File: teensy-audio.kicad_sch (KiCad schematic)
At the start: 44 parts, among them J1 AudioJack2, J2 AudioJack2, J3 Barrel_Jack, J4 Conn_02x08_Odd_Even, J5 Conn_02x08_Odd_Even, J6 Conn_02x05_Odd_Even, J7 Conn_01x04, SW1 RotaryEncoder_Switch, SW2 SW_Push, SW3 SW_Push, SW4 SW_Push, SW5 SW_Push, U1 LM358, U2 LM7805_TO220, U3 Teensy4.0, U4 Teensy4.0_AudioShield_REVD

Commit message: added power connectors
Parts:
- added J10: Conn_01x05, Connector_PinHeader_2.54mm:PinHeader_1x05_P2.54mm_Vertical, symbol Connector_Generic:Conn_01x05
- added J8: Conn_01x04, Connector_PinHeader_2.54mm:PinHeader_1x04_P2.54mm_Vertical, symbol Connector_Generic:Conn_01x04
- added J9: Conn_02x05_Odd_Even, Connector_PinHeader_2.54mm:PinHeader_2x05_P2.54mm_Vertical, symbol Connector_Generic:Conn_02x05_Odd_Even
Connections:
- net +3.3V: now also J9.1 (Pin_1), J9.3 (Pin_3), J9.5 (Pin_5), J9.7 (Pin_7), J9.9 (Pin_9)
- net +5V: now also J9.10 (Pin_10), J9.2 (Pin_2), J9.4 (Pin_4), J9.6 (Pin_6), J9.8 (Pin_8)
- net GND: now also J10.1 (Pin_1), J10.2 (Pin_2), J10.3 (Pin_3), J10.4 (Pin_4), J10.5 (Pin_5)
- net MISO: now also J8.3 (Pin_3)
- net MOSI: now also J8.2 (Pin_2)
- net SCK: now also J8.4 (Pin_4)
- net SDCS: now also J8.1 (Pin_1)

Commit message: finished pcb
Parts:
- J1, J2: footprint Connector_Audio:Jack_6.35mm_Neutrik_NMJ4HFD2_Horizontal -> Connector_Audio:Jack_6.35mm_Neutrik_NMJ6HFD2-AU_Horizontal
- J3: footprint Connector_BarrelJack:BarrelJack_CUI_PJ-063AH_Horizontal -> Connector_BarrelJack:BarrelJack_GCT_DCJ200-10-A_Horizontal
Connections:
- net GND: now also J3.1; no longer J3.2
- net VCC: now also J3.2; no longer J3.1
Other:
- moved on the sheet: J3
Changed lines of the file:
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@@
     (stroke (width 0) (type default))
   )
-  (wire (pts (xy 154.94 34.29) (xy 158.75 34.29))
-    (stroke (width 0) (type default))
-  )
   (wire (pts (xy 133.35 151.13) (xy 139.7 151.13))
     (stroke (width 0) (type default))
@@
     (stroke (width 0) (type default))
   )
-  (wire (pts (xy 261.62 31.75) (xy 261.62 34.29))
+  (wire (pts (xy 261.62 33.02) (xy 261.62 34.29))
     (stroke (width 0) (type default))
   )
@@
     (stroke (width 0) (type default))
   )
+  (wire (pts (xy 261.62 24.13) (xy 261.62 27.94))
+    (stroke (width 0) (type default))
+  )
   (wire (pts (xy 123.19 87.63) (xy 123.19 96.52))
     (stroke (width 0) (type default))
@@
     (stroke (width 0) (type default))
   )
-  (wire (pts (xy 261.62 26.67) (xy 261.62 24.13))
-    (stroke (width 0) (type default))
-  )
   (wire (pts (xy 274.32 77.47) (xy 278.13 77.47))
     (stroke (width 0) (type default))
@@
     (stroke (width 0) (type default))
   )
+  (wire (pts (xy 261.62 27.94) (xy 267.97 27.94))
+    (stroke (width 0) (type default))
+  )
   (wire (pts (xy 92.71 91.44) (xy 92.71 93.98))
     (stroke (width 0) (type default))
@@
     (stroke (width 0) (type default))
   )
-  (wire (pts (xy 179.07 99.06) (xy 182.88 99.06))
+  (wire (pts (xy 154.94 34.29) (xy 158.75 34.29))
     (stroke (width 0) (type default))
   )
-  (wire (pts (xy 259.08 26.67) (xy 261.62 26.67))
+  (wire (pts (xy 179.07 99.06) (xy 182.88 99.06))
     (stroke (width 0) (type default))
   )
@@
     (stroke (width 0) (type default))
   )
+  (wire (pts (xy 267.97 33.02) (xy 261.62 33.02))
+    (stroke (width 0) (type default))
+  )
   (wire (pts (xy 130.81 83.82) (xy 130.81 81.28))
     (stroke (width 0) (type default))
@@
     (stroke (width 0) (type default))
   )
-  (wire (pts (xy 259.08 31.75) (xy 261.62 31.75))
-    (stroke (width 0) (type default))
-  )
   (wire (pts (xy 182.88 73.66) (xy 168.91 73.66))
     (stroke (width 0) (type default))
@@
     )
   )
-  (symbol (lib_id "Connector:Barrel_Jack") (at 251.46 29.21 0) (unit 1)
+  (symbol (lib_id "Connector:Barrel_Jack") (at 275.59 30.48 180) (unit 1)
     (in_bom yes) (on_board yes) (dnp no) (fields_autoplaced)
-    (property "Reference" "J3" (at 251.46 20.32 0)
-      (effects (font (size 1.27 1.27)))
+    (property "Reference" "J3" (at 281.94 29.21 0)
+      (effects (font (size 1.27 1.27)) (justify right))
     )
-    (property "Value" "Barrel_Jack" (at 251.46 22.86 0)
-      (effects (font (size 1.27 1.27)))
+    (property "Value" "Barrel_Jack" (at 281.94 31.75 0)
+      (effects (font (size 1.27 1.27)) (justify right))
     )
-    (property "Footprint" "Connector_BarrelJack:BarrelJack_CUI_PJ-063AH_Horizontal" (at 252.73 30.226 0)
+    (property "Footprint" "Connector_BarrelJack:BarrelJack_GCT_DCJ200-10-A_Horizontal" (at 274.32 29.464 0)
       (effects (font (size 1.27 1.27)) hide)
     )
-    (property "Datasheet" "~" (at 252.73 30.226 0)
+    (property "Datasheet" "~" (at 274.32 29.464 0)
       (effects (font (size 1.27 1.27)) hide)
     )
@@
       (effects (font (size 1.27 1.27)))
     )
-    (property "Footprint" "Connector_Audio:Jack_6.35mm_Neutrik_NMJ4HFD2_Horizontal" (at 24.13 24.13 0)
+    (property "Footprint" "Connector_Audio:Jack_6.35mm_Neutrik_NMJ6HFD2-AU_Horizontal" (at 24.13 24.13 0)
       (effects (font (size 1.27 1.27)) hide)
     )
@@
       (effects (font (size 1.27 1.27)))
     )
-    (property "Footprint" "Connector_Audio:Jack_6.35mm_Neutrik_NMJ4HFD2_Horizontal" (at 166.37 34.29 0)
+    (property "Footprint" "Connector_Audio:Jack_6.35mm_Neutrik_NMJ6HFD2-AU_Horizontal" (at 166.37 34.29 0)
       (effects (font (size 1.27 1.27)) hide)
     )

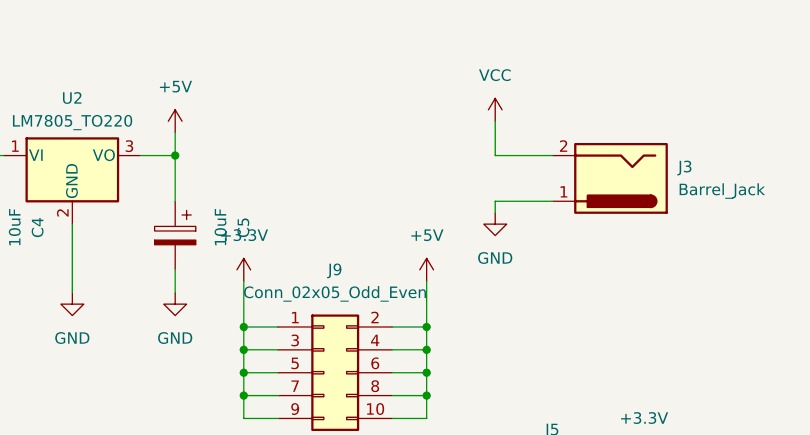
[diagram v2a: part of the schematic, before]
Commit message: added input power pins
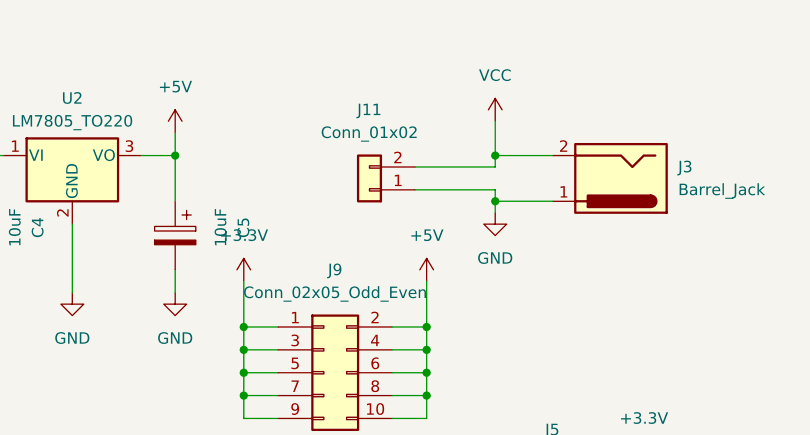
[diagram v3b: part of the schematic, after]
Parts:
- added J11: Conn_01x02, Connector_PinHeader_2.54mm:PinHeader_1x02_P2.54mm_Vertical, symbol Connector_Generic:Conn_01x02
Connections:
- net GND: now also J11.1 (Pin_1)
- net VCC: now also J11.2 (Pin_2)
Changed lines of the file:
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@@
   (junction (at 31.75 66.04) (diameter 0) (color 0 0 0 0)
   )
+  (junction (at 261.62 33.02) (diameter 0) (color 0 0 0 0)
+  )
   (junction (at 27.94 161.29) (diameter 0) (color 0 0 0 0)
   )
@@
   (junction (at 72.39 36.83) (diameter 0) (color 0 0 0 0)
   )
+  (junction (at 261.62 27.94) (diameter 0) (color 0 0 0 0)
+  )
   (junction (at 237.49 64.77) (diameter 0) (color 0 0 0 0)
   )
@@
     (stroke (width 0) (type default))
   )
+  (wire (pts (xy 252.73 31.75) (xy 261.62 31.75))
+    (stroke (width 0) (type default))
+  )
   (wire (pts (xy 22.86 182.88) (xy 26.67 182.88))
     (stroke (width 0) (type default))
@@
     (stroke (width 0) (type default))
   )
+  (wire (pts (xy 252.73 29.21) (xy 261.62 29.21))
+    (stroke (width 0) (type default))
+  )
   (wire (pts (xy 238.76 149.86) (xy 254 149.86))
     (stroke (width 0) (type default))
@@
     (stroke (width 0) (type default))
   )
+  (wire (pts (xy 261.62 29.21) (xy 261.62 27.94))
+    (stroke (width 0) (type default))
+  )
   (wire (pts (xy 38.1 161.29) (xy 33.02 161.29))
     (stroke (width 0) (type default))
@@
     (stroke (width 0) (type default))
   )
+  (wire (pts (xy 261.62 31.75) (xy 261.62 33.02))
+    (stroke (width 0) (type default))
+  )
   (wire (pts (xy 134.62 87.63) (xy 135.89 87.63))
     (stroke (width 0) (type default))
@@
   )
   (symbol (lib_id "teensy4.0_audioshield_revd:Teensy4.0_AudioShield_REVD") (at 105.41 154.94 0) (unit 1)
-    (in_bom yes) (on_board yes) (dnp no) (fields_autoplaced)
+    (in_bom yes) (on_board no) (dnp no) (fields_autoplaced)
     (property "Reference" "U4" (at 105.41 113.03 0)
       (effects (font (size 1.27 1.27)))
@@
         )
       )
+    )
+  )
+  (symbol (lib_id "Connector_Generic:Conn_01x02") (at 247.65 31.75 180) (unit 1)
+    (in_bom yes) (on_board yes) (dnp no) (fields_autoplaced)
+    (property "Reference" "J11" (at 247.65 22.86 0)
+      (effects (font (size 1.27 1.27)))
+    )
+    (property "Value" "Conn_01x02" (at 247.65 25.4 0)
+      (effects (font (size 1.27 1.27)))
+    )
+    (property "Footprint" "Connector_PinHeader_2.54mm:PinHeader_1x02_P2.54mm_Vertical" (at 247.65 31.75 0)
+      (effects (font (size 1.27 1.27)) hide)
+    )
+    (property "Datasheet" "~" (at 247.65 31.75 0)
+      (effects (font (size 1.27 1.27)) hide)
+    )
+    (pin "1")
+    (pin "2")
+    (instances
+      (project "teensy-audio"
+        (path "/6ae84b48-cfd0-4085-8818-9f5b4e5692b2"
+          (reference "J11") (unit 1)
+        )
+      )

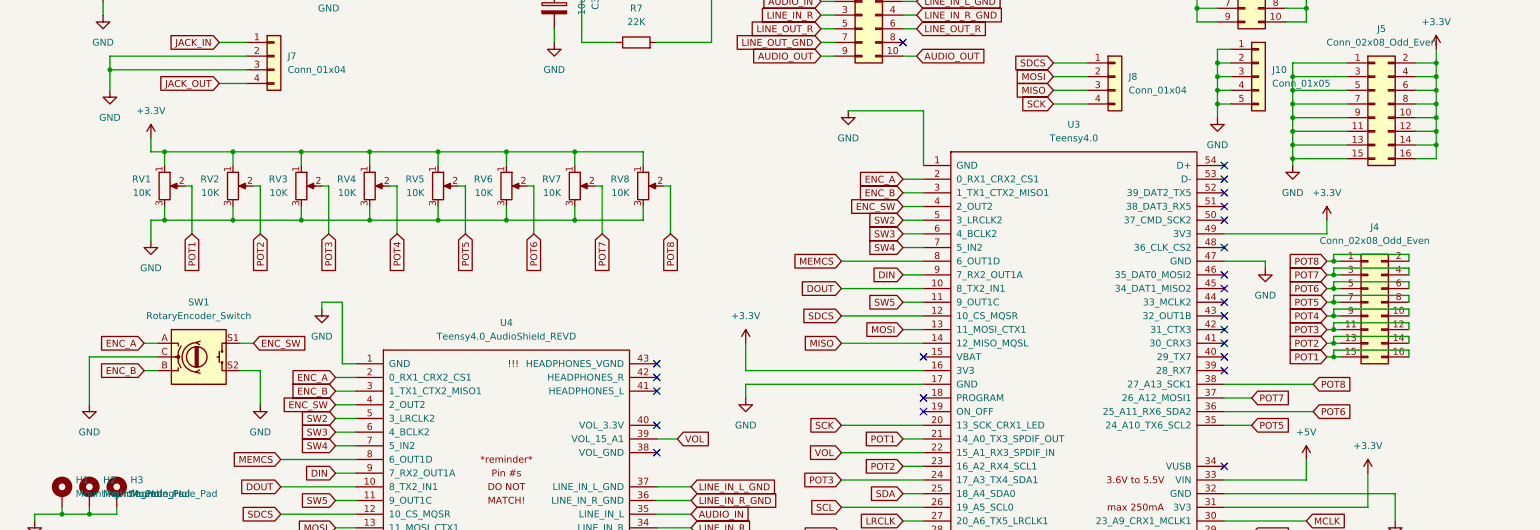
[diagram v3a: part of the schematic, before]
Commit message: added oled screen
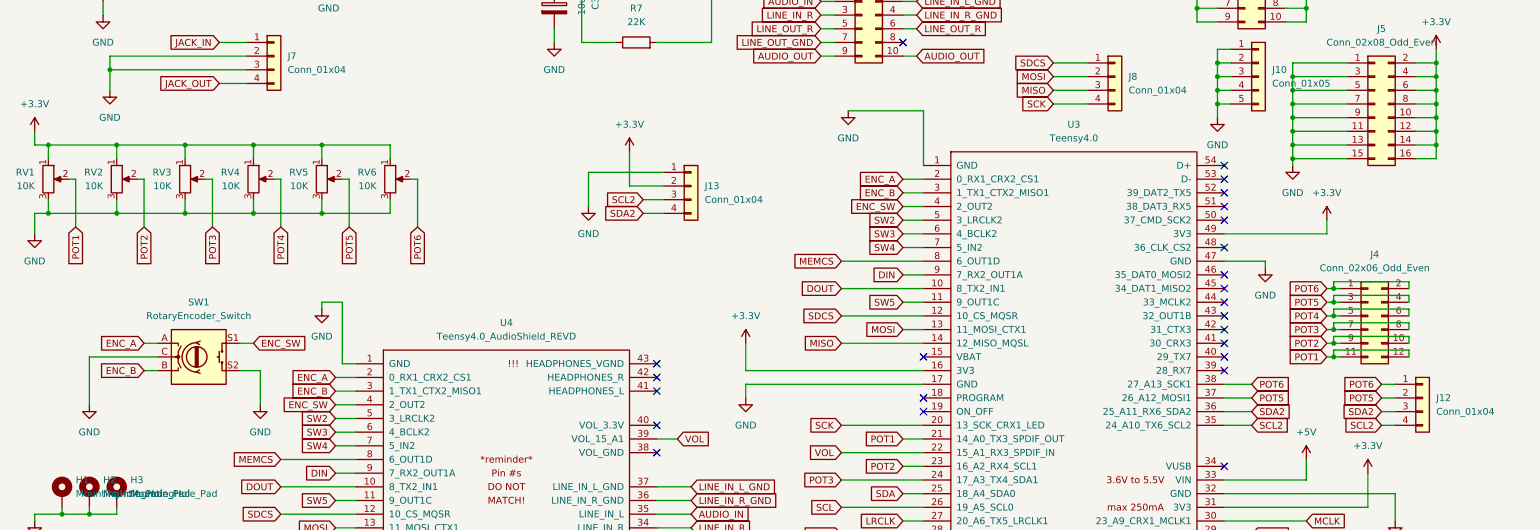
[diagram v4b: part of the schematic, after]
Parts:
- removed J4: Conn_02x08_Odd_Even, Connector_PinHeader_2.54mm:PinHeader_2x08_P2.54mm_Vertical, symbol Connector_Generic:Conn_02x08_Odd_Even
- removed RV7, RV8: 10K, Potentiometer_THT:Potentiometer_Bourns_PTV09A-1_Single_Vertical, symbol Device:R_Potentiometer
- added J12, J13: Conn_01x04, Connector_PinHeader_2.54mm:PinHeader_1x04_P2.54mm_Vertical, symbol Connector_Generic:Conn_01x04
- added J4: Conn_02x06_Odd_Even, Connector_PinHeader_2.54mm:PinHeader_2x06_P2.54mm_Vertical, symbol Connector_Generic:Conn_02x06_Odd_Even
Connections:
- net POT7 is gone; now on net POT5: U3.37 (26_A12_MOSI1)
- net POT8 is gone; now on net POT6: U3.38 (27_A13_SCK1)
- net +3.3V: now also J13.2 (Pin_2)
- net GND: now also J13.1 (Pin_1)
- net POT1: now also J4.11 (Pin_11), J4.12 (Pin_12)
- net POT2: now also J4.10 (Pin_10), J4.9 (Pin_9)
- net POT3: now also J4.7 (Pin_7), J4.8 (Pin_8)
- net POT4: now also J4.5 (Pin_5), J4.6 (Pin_6)
- net POT5: now also J12.2 (Pin_2), J4.3 (Pin_3), J4.4 (Pin_4); no longer U3.35 (24_A10_TX6_SCL2)
- net POT6: now also J12.1 (Pin_1), J4.1 (Pin_1), J4.2 (Pin_2); no longer U3.36 (25_A11_RX6_SDA2)
- new net SCL2: J12.4 (Pin_4), J13.3 (Pin_3), U3.35 (24_A10_TX6_SCL2)
- new net SDA2: J12.3 (Pin_3), J13.4 (Pin_4), U3.36 (25_A11_RX6_SDA2)
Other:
- moved on the sheet: RV1, RV2, RV3, RV4, RV5, RV6

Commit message: split audio and digital grounds
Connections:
- net LINE_IN_R_GND is gone; now on net GNDA: J6.4 (Pin_4), U4.36 (LINE_IN_R_GND)
- net LINE_OUT_GND is gone; now on net GNDA: J6.7 (Pin_7), U4.32 (LINE_OUT_GND)
- net GND: no longer C3.2, J1.S, J2.S, J7.2 (Pin_2), J7.3 (Pin_3), R2.2, R4.2, R5.2, U1.4 (V-)
- net LINE_IN_L_GND renamed GNDA
- net GNDA: now also C3.2, J1.S, J2.S, J7.2 (Pin_2), J7.3 (Pin_3), R2.2, R4.2, R5.2, U1.4 (V-)

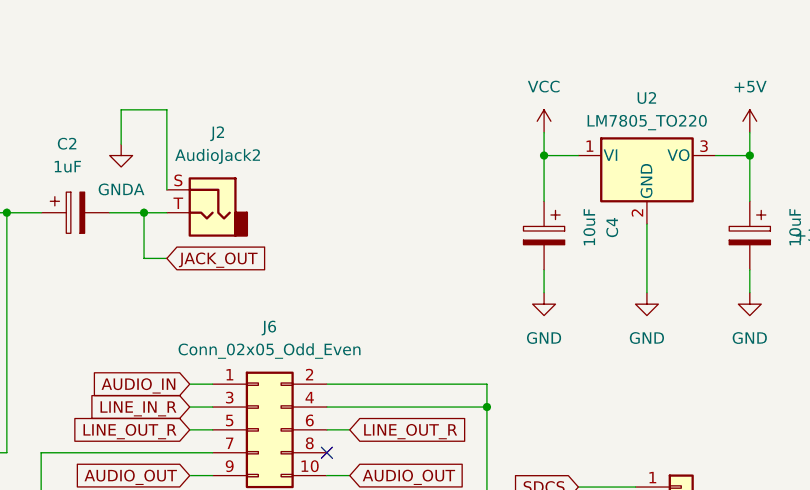
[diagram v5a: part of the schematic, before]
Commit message: decoupling capacitor for audio opamp
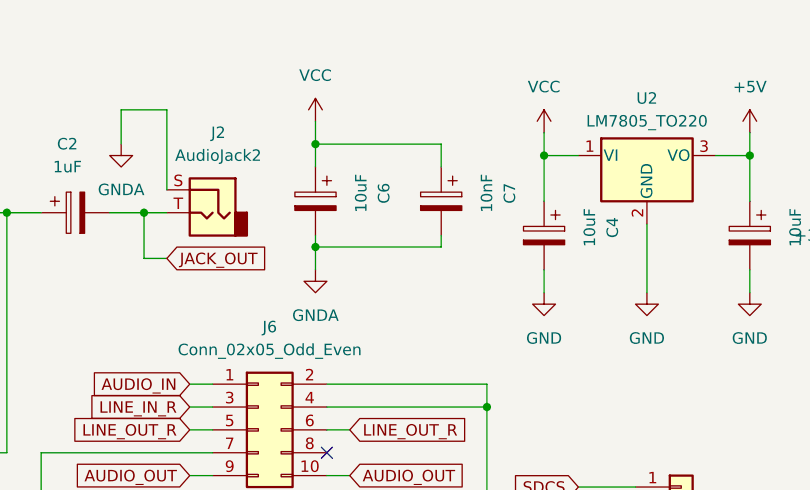
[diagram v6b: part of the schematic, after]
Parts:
- added C6: 10uF, Capacitor_THT:CP_Radial_D4.0mm_P2.00mm, symbol Device:C_Polarized
- added C7: 10nF, Capacitor_THT:CP_Radial_D4.0mm_P2.00mm, symbol Device:C_Polarized
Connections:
- net GNDA: now also C6.2, C7.2
- net VCC: now also C6.1, C7.1
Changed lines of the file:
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@@
   (junction (at 278.13 80.01) (diameter 0) (color 0 0 0 0)
   )
+  (junction (at 177.8 26.67) (diameter 0) (color 0 0 0 0)
+  )
   (junction (at 278.13 67.31) (diameter 0) (color 0 0 0 0)
   )
@@
   (junction (at 233.68 46.99) (diameter 0) (color 0 0 0 0)
   )
+  (junction (at 177.8 38.1) (diameter 0) (color 0 0 0 0)
+  )
   (junction (at 254 52.07) (diameter 0) (color 0 0 0 0)
   )
@@
     (stroke (width 0) (type default))
   )
+  (wire (pts (xy 191.77 26.67) (xy 177.8 26.67))
+    (stroke (width 0) (type default))
+  )
   (wire (pts (xy 222.25 27.94) (xy 226.06 27.94))
     (stroke (width 0) (type default))
@@
     (stroke (width 0) (type default))
   )
+  (wire (pts (xy 191.77 38.1) (xy 177.8 38.1))
+    (stroke (width 0) (type default))
+  )
   (wire (pts (xy 254 54.61) (xy 254 52.07))
     (stroke (width 0) (type default))
@@
     (stroke (width 0) (type default))
   )
+  (wire (pts (xy 177.8 26.67) (xy 177.8 29.21))
+    (stroke (width 0) (type default))
+  )
   (wire (pts (xy 167.64 111.76) (xy 182.88 111.76))
     (stroke (width 0) (type default))
@@
     (stroke (width 0) (type default))
   )
+  (wire (pts (xy 177.8 38.1) (xy 177.8 40.64))
+    (stroke (width 0) (type default))
+  )
   (wire (pts (xy 273.05 105.41) (xy 259.08 105.41))
     (stroke (width 0) (type default))
@@
     (stroke (width 0) (type default))
   )
+  (wire (pts (xy 191.77 29.21) (xy 191.77 26.67))
+    (stroke (width 0) (type default))
+  )
   (wire (pts (xy 179.07 86.36) (xy 182.88 86.36))
     (stroke (width 0) (type default))
@@
     (stroke (width 0) (type default))
   )
+  (wire (pts (xy 177.8 36.83) (xy 177.8 38.1))
+    (stroke (width 0) (type default))
+  )
   (wire (pts (xy 22.86 172.72) (xy 26.67 172.72))
     (stroke (width 0) (type default))
@@
     (stroke (width 0) (type default))
   )
+  (wire (pts (xy 177.8 24.13) (xy 177.8 26.67))
+    (stroke (width 0) (type default))
+  )
   (wire (pts (xy 196.85 55.88) (xy 196.85 67.31))
     (stroke (width 0) (type default))
@@
     (stroke (width 0) (type default))
   )
+  (wire (pts (xy 191.77 36.83) (xy 191.77 38.1))
+    (stroke (width 0) (type default))
+  )
   (wire (pts (xy 33.02 160.02) (xy 33.02 161.29))
     (stroke (width 0) (type default))
@@
     )
   )
+  (symbol (lib_id "Device:C_Polarized") (at 177.8 33.02 0) (mirror y) (unit 1)
+    (in_bom yes) (on_board yes) (dnp no)
+    (property "Reference" "C6" (at 185.42 32.131 90)
+      (effects (font (size 1.27 1.27)))
+    )
+    (property "Value" "10uF" (at 182.88 32.131 90)
+      (effects (font (size 1.27 1.27)))
+    )
+    (property "Footprint" "Capacitor_THT:CP_Radial_D4.0mm_P2.00mm" (at 176.8348 36.83 0)
+      (effects (font (size 1.27 1.27)) hide)
+    )
+    (property "Datasheet" "~" (at 177.8 33.02 0)
+      (effects (font (size 1.27 1.27)) hide)
+    )
+    (pin "1")
+    (pin "2")
+    (instances
+      (project "teensy-audio"
+        (path "/6ae84b48-cfd0-4085-8818-9f5b4e5692b2"
+          (reference "C6") (unit 1)
+        )
+      )
+    )
+  )
   (symbol (lib_id "Device:R") (at 30.48 49.53 0) (unit 1)
     (in_bom yes) (on_board yes) (dnp no) (fields_autoplaced)
@@
     )
   )
+  (symbol (lib_id "Device:C_Polarized") (at 191.77 33.02 0) (mirror y) (unit 1)
+    (in_bom yes) (on_board yes) (dnp no)
+    (property "Reference" "C7" (at 199.39 32.131 90)
+      (effects (font (size 1.27 1.27)))
+    )
+    (property "Value" "10nF" (at 196.85 32.131 90)
+      (effects (font (size 1.27 1.27)))
+    )
+    (property "Footprint" "Capacitor_THT:CP_Radial_D4.0mm_P2.00mm" (at 190.8048 36.83 0)
+      (effects (font (size 1.27 1.27)) hide)
+    )
+    (property "Datasheet" "~" (at 191.77 33.02 0)
+      (effects (font (size 1.27 1.27)) hide)
+    )
+    (pin "1")
+    (pin "2")
+    (instances
+      (project "teensy-audio"
+        (path "/6ae84b48-cfd0-4085-8818-9f5b4e5692b2"
+          (reference "C7") (unit 1)
+        )
+      )
+    )
+  )
   (symbol (lib_id "power:GND") (at 203.2 43.18 0) (unit 1)
     (in_bom yes) (on_board yes) (dnp no) (fields_autoplaced)
@@
     )
   )
+  (symbol (lib_id "power:VCC") (at 177.8 24.13 0) (unit 1)
+    (in_bom yes) (on_board yes) (dnp no) (fields_autoplaced)
+    (property "Reference" "#PWR048" (at 177.8 27.94 0)
+      (effects (font (size 1.27 1.27)) hide)
+    )
+    (property "Value" "VCC" (at 177.8 19.05 0)
+      (effects (font (size 1.27 1.27)))
+    )
+    (property "Footprint" "" (at 177.8 24.13 0)
+      (effects (font (size 1.27 1.27)) hide)
+    )
+    (property "Datasheet" "" (at 177.8 24.13 0)
+      (effects (font (size 1.27 1.27)) hide)
+    )
+    (pin "1")
+    (instances
+      (project "teensy-audio"
+        (path "/6ae84b48-cfd0-4085-8818-9f5b4e5692b2"
+          (reference "#PWR048") (unit 1)
+        )
+      )
+    )
+  )
   (symbol (lib_id "power:+5V") (at 254 138.43 0) (unit 1)
     (in_bom yes) (on_board yes) (dnp no) (fields_autoplaced)
@@
         )
       )
+    )
+  )
+  (symbol (lib_id "power:GNDA") (at 177.8 40.64 0) (unit 1)
+    (in_bom yes) (on_board yes) (dnp no) (fields_autoplaced)
+    (property "Reference" "#PWR047" (at 177.8 46.99 0)
+      (effects (font (size 1.27 1.27)) hide)
+    )
+    (property "Value" "GNDA" (at 177.8 45.72 0)
+      (effects (font (size 1.27 1.27)))
+    )
+    (property "Footprint" "" (at 177.8 40.64 0)
+      (effects (font (size 1.27 1.27)) hide)
+    )
+    (property "Datasheet" "" (at 177.8 40.64 0)
+      (effects (font (size 1.27 1.27)) hide)
+    )
+    (pin "1")
+    (instances
+      (project "teensy-audio"
+        (path "/6ae84b48-cfd0-4085-8818-9f5b4e5692b2"
+          (reference "#PWR047") (unit 1)
+        )
+      )
